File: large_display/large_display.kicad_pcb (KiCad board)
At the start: 2 copper layers, 92 x 100 mm, 138 parts, among them J1 Conn_01x11, J2 Conn_01x11, U1 TLC5940PWP, U2 74HC244

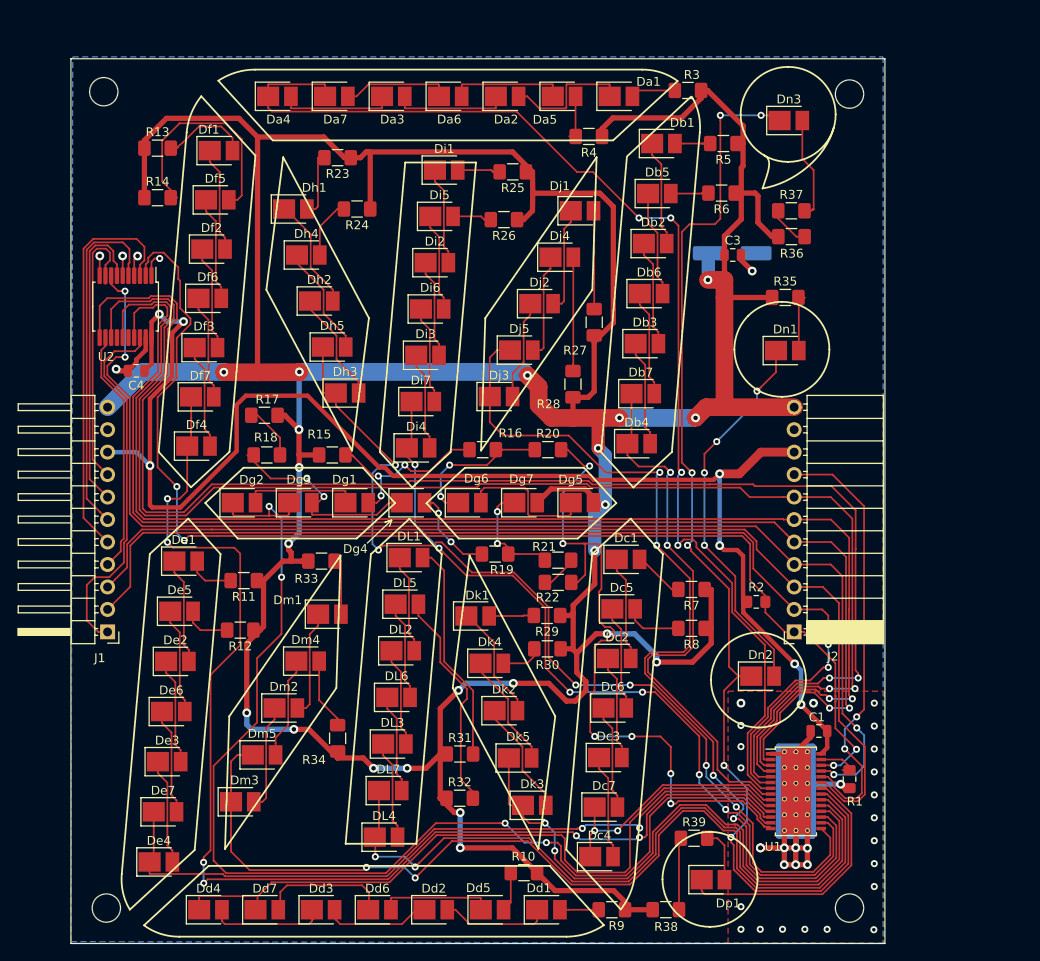
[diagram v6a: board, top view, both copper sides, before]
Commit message: add a bit of clearance between segment outlines and nearest components for light dam
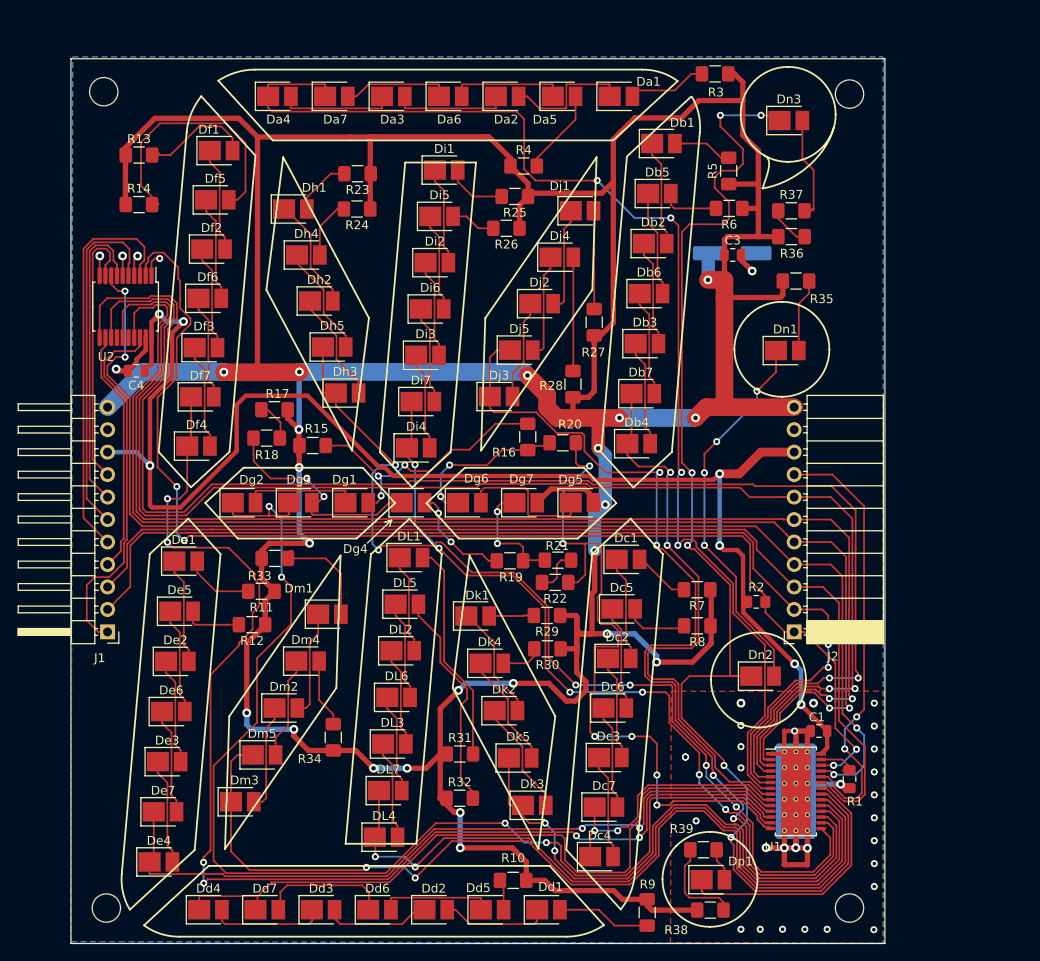
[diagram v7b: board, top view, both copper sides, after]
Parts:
- moved R4 8.10 mm to (101.2, 62.1), turned to 0 degrees
- moved R16 5.29 mm to (101.6, 92.7), turned to 270 degrees
- moved R33 5.28 mm to (73.0, 106.5)
- moved R38 5.03 mm to (122.3, 146.2)
- moved R9 4.00 mm to (115.1, 146.5), turned to 270 degrees
- moved R3 3.59 mm to (122.8, 51.7)
- moved R5 3.15 mm to (124.3, 62.7), turned to 90 degrees
- moved R23 2.89 mm to (82.4, 63.0)
- moved R25 2.79 mm to (100.2, 65.6)
- moved R15 2.47 mm to (77.3, 93.7)
- moved R11 2.33 mm to (71.5, 110.2)
- moved R13 2.24 mm to (57.7, 60.9)
- moved R14 2.24 mm to (57.7, 66.5)
- moved R35 2.22 mm to (131.9, 75.1)
- moved R6 1.93 mm to (124.4, 66.9)
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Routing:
- net Vdrive: track 500.6 -> 526.2 mm
- net Net-(Dn2-Pad1): track 128.8 -> 141.8 mm
- net GND: track 93.6 -> 104.3 mm, vias 36 -> 35
- net Net-(Dg1-Pad2): track 21.4 -> 31.6 mm
- net Net-(Dd1-Pad2): track 4.39 -> 10.6 mm
- net Net-(Dm1-Pad2): track 6.75 -> 12.3 mm
- net Net-(Da5-Pad2): track 4.83 -> 9.69 mm
- net Net-(Da1-Pad2): track 5.06 -> 8.91 mm
- net Net-(Df5-Pad2): track 26.4 -> 29.9 mm
- net Net-(Df1-Pad2): track 10.2 -> 13.5 mm
- net Net-(Da4-Pad1): track 134.7 -> 138.0 mm
- net Net-(R38-Pad2): track 8.16 -> 10.8 mm
- net Net-(R20-Pad2): track 77.0 -> 79.6 mm
- net Net-(Db1-Pad2): track 4.17 -> 6.74 mm
- net Net-(De1-Pad2): track 5.46 -> 7.95 mm
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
